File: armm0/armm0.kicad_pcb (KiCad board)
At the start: 2 copper layers, 76.2 x 52.1 mm, 10 parts, among them J1 Conn_02x10_Odd_Even, J2 Conn_02x24_Odd_Even, J3 Conn_02x24_Odd_Even, U1 STM32F070F6Px, U2 LD1117S33TR_SOT223

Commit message: armm0: Add eagle project
Signed-off-by: Ben <bdl@live.co.uk>
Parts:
- J2, J3: moved to B.Cu
- R1, R2: moved to F.Cu
- moved J2 3.81 mm to (32.4, 76.8), turned to 270 degrees
- moved C3 2.17 mm to (91.9, 52.1), turned to 0 degrees
- moved J3 1.91 mm to (32.4, 34.9), turned to 270 degrees
- turned R1 to 90 degrees
- turned R2 to 90 degrees
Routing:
- net +3V3: track 40.7 -> 9.36 mm, vias 2 -> 0
- net I2C1_SCL: track 11.3 -> 1.68 mm
- net I2C1_SDA: track 3.63 -> 1.68 mm
- net (no net): vias 1 -> 0
- added copper zone on F.Cu, net +3V3
- added copper zone on B.Cu, net GND

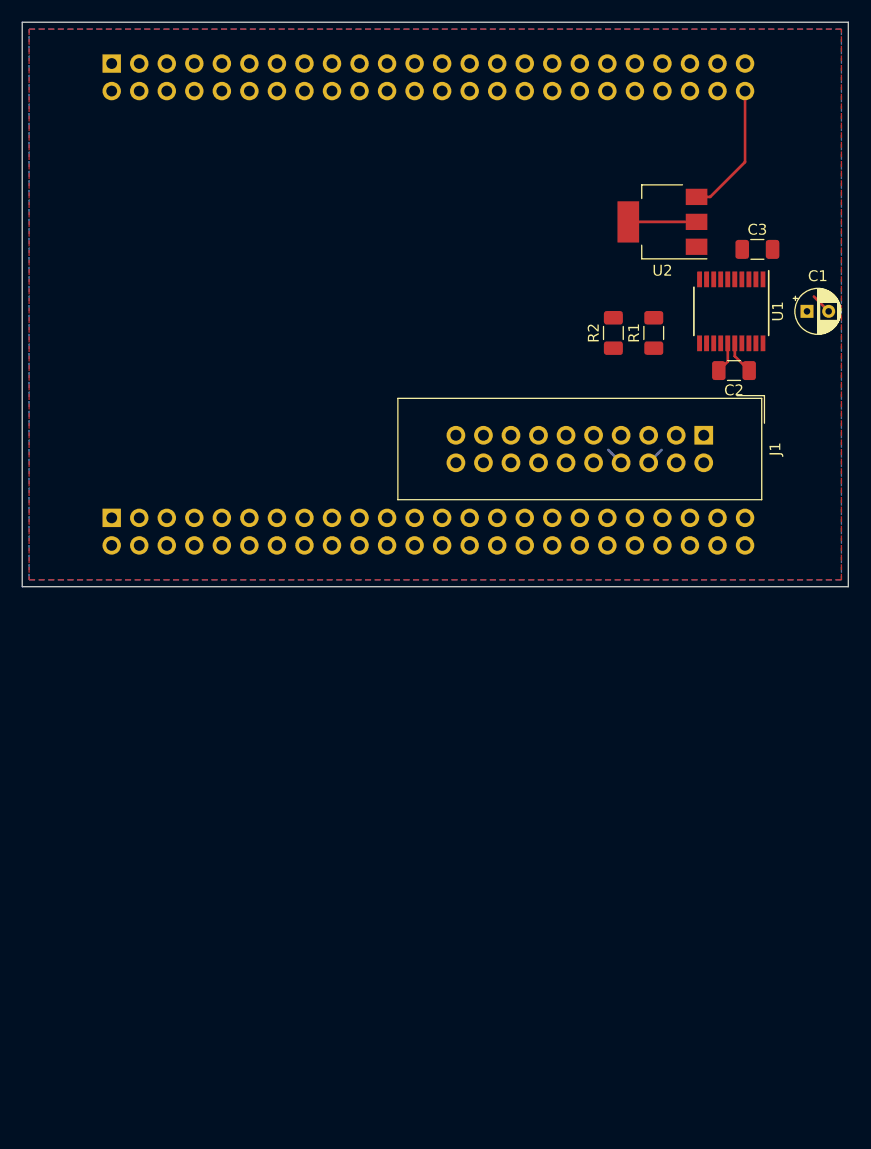
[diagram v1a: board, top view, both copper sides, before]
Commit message: sch: Add Conn_02x08 for shorter board
Signed-off-by: Ben Lancaster <bdl@live.co.uk>
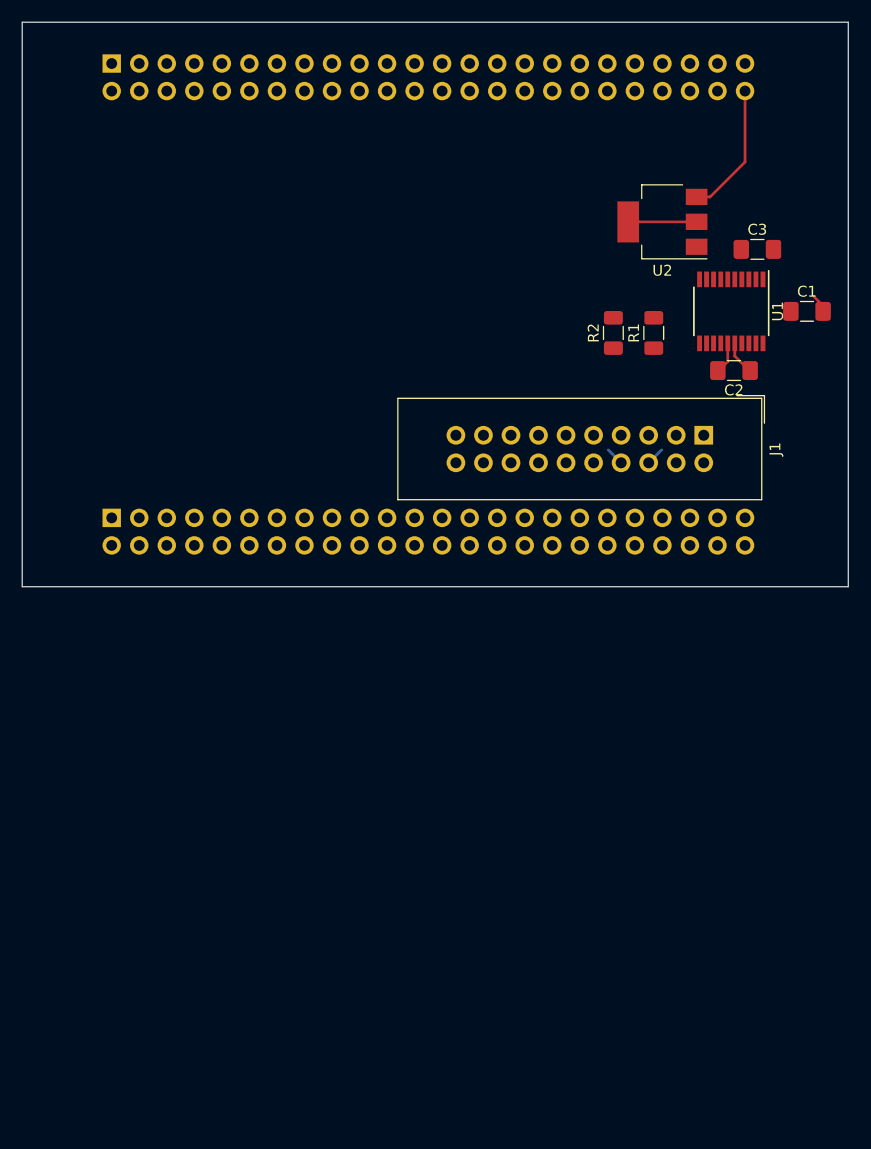
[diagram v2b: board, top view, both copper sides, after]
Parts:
- C1: footprint Capacitor_THT:CP_Radial_D4.0mm_P2.00mm -> Capacitor_SMD:C_1206_3216Metric_Pad1.42x1.75mm_HandSolder
- C2, C3: footprint Capacitor_SMD:C_1206_3216Metric -> Capacitor_SMD:C_1206_3216Metric_Pad1.42x1.75mm_HandSolder
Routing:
- removed copper zone on F.Cu, net +3V3
- removed copper zone on B.Cu, net GND

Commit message: sch: Flip Conn_02x08 pin headers for upside down insertion to master board
Signed-off-by: Ben Lancaster <bdl@live.co.uk>
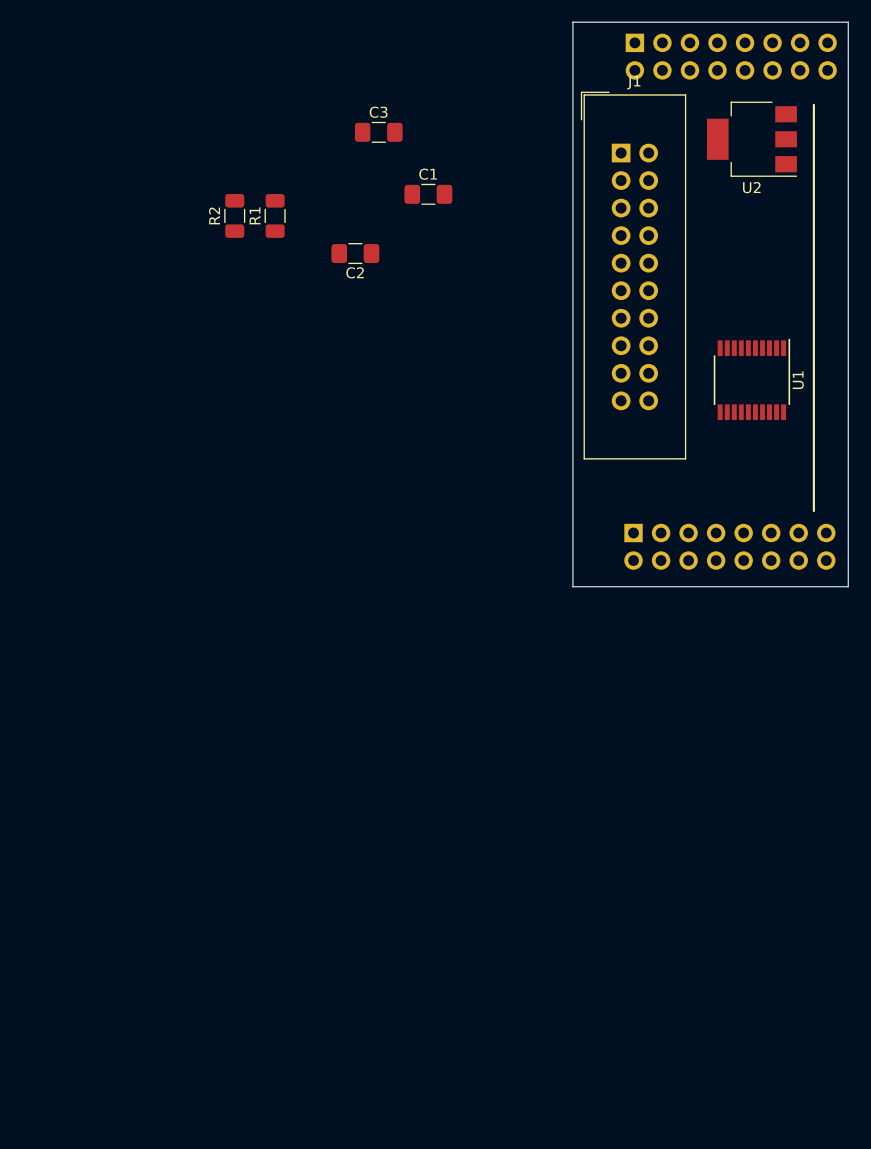
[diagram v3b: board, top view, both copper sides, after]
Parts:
- removed J2, J3: Conn_02x24_Odd_Even, Connector_PinHeader_2.54mm:PinHeader_2x24_P2.54mm_Vertical
- added J4: Conn_02x08_Odd_Even, Connector_PinHeader_2.54mm:PinHeader_2x08_P2.54mm_Vertical, B.Cu at (80.5, 78.2)
- added J5: Conn_02x08_Odd_Even, Connector_PinHeader_2.54mm:PinHeader_2x08_P2.54mm_Vertical, B.Cu at (80.6, 33.0)
- moved C2 36.6 mm to (54.9, 52.5)
- moved R1 36.6 mm to (47.5, 49.0)
- moved R2 36.6 mm to (43.7, 49.0)
- moved C1 36.6 mm to (61.6, 47.0)
- moved C3 36.6 mm to (57.0, 41.3)
- moved J1 27.1 mm to (79.4, 43.2), turned to 0 degrees
- moved U2 11.2 mm to (91.4, 41.9)
- moved U1 6.63 mm to (91.4, 64.1)
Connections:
- net Net-(J1-Pad13) renamed JTAG_TDI
- net Net-(J1-Pad3) renamed JTAG_TRST
- net Net-(J1-Pad5) renamed JTAG_TDO
- net Net-(U1-Pad6) renamed ADC_IN0
- net Net-(U1-Pad7) renamed ADC_IN1
- J1 pad 1: Net-(J1-Pad1) -> +3V3
- J1 pad 10: Net-(J1-Pad10) -> GND
- J1 pad 12: Net-(J1-Pad12) -> GND
- J1 pad 14: Net-(J1-Pad14) -> GND
- J1 pad 15: Net-(J1-Pad15) -> NRST
- J1 pad 16: Net-(J1-Pad16) -> GND
- J1 pad 18: Net-(J1-Pad18) -> GND
- J1 pad 19: Net-(J1-Pad19) -> +3V3
- J1 pad 2: SWDIO -> +3V3
- J1 pad 20: Net-(J1-Pad20) -> GND
- J1 pad 4: SWCLK -> GND
- J1 pad 6: I2C1_SDA -> GND
- J1 pad 7: Net-(J1-Pad7) -> SWDIO
- J1 pad 8: I2C1_SCL -> GND
- J1 pad 9: Net-(J1-Pad9) -> SWCLK
- R1 pad 2: I2C1_SDA -> C7
- R2 pad 2: I2C1_SCL -> C9
- U1 pad 2: I2C1_SDA -> C7
- U1 pad 3: I2C1_SCL -> C9
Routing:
- net +5V: track 13.0 -> 0.00 mm
- net +3V3: track 9.36 -> 0.00 mm
- net GND: track 4.78 -> 0.00 mm
- net I2C1_SCL: track 1.68 -> 0.00 mm
- net I2C1_SDA: track 1.68 -> 0.00 mm
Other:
- board size 76.2 x 52.1 mm -> 25.4 x 52.1 mm

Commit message: sch: Switch between board or stlink power source with 3pin selector
Signed-off-by: Ben Lancaster <bdl@live.co.uk>
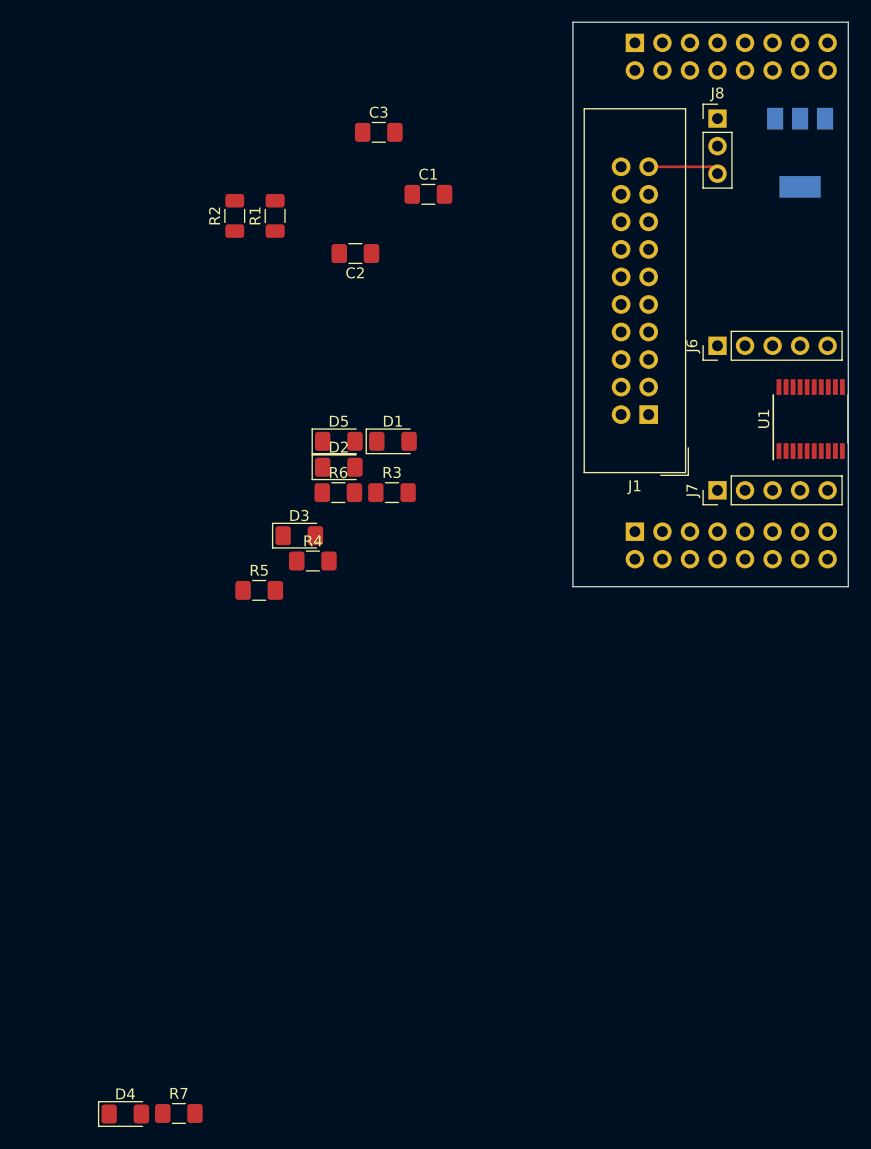
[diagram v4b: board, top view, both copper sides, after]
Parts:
- added D1: LED, LED_SMD:LED_1206_3216Metric_Pad1.42x1.75mm_HandSolder, F.Cu at (58.3, 69.8)
- added D2: LED, LED_SMD:LED_1206_3216Metric_Pad1.42x1.75mm_HandSolder, F.Cu at (53.3, 72.2)
- added D3: LED, LED_SMD:LED_1206_3216Metric_Pad1.42x1.75mm_HandSolder, F.Cu at (49.7, 78.5)
- added D4: LED, LED_SMD:LED_1206_3216Metric_Pad1.42x1.75mm_HandSolder, F.Cu at (33.6, 131.8)
- added D5: LED, LED_SMD:LED_1206_3216Metric_Pad1.42x1.75mm_HandSolder, F.Cu at (53.3, 69.8)
- added J6: Conn_01x05_Male, Connector_PinHeader_2.54mm:PinHeader_1x05_P2.54mm_Vertical, F.Cu at (88.3, 61.0)
- added J7: Conn_01x05_Male, Connector_PinHeader_2.54mm:PinHeader_1x05_P2.54mm_Vertical, F.Cu at (88.3, 74.3)
- added J8: Conn_01x03_Male, Connector_PinHeader_2.54mm:PinHeader_1x03_P2.54mm_Vertical, F.Cu at (88.3, 40.0)
- added R3: R, Resistor_SMD:R_1206_3216Metric_Pad1.42x1.75mm_HandSolder, F.Cu at (58.2, 74.5)
- added R4: R, Resistor_SMD:R_1206_3216Metric_Pad1.42x1.75mm_HandSolder, F.Cu at (50.9, 80.8)
- added R5: R, Resistor_SMD:R_1206_3216Metric_Pad1.42x1.75mm_HandSolder, F.Cu at (46.0, 83.5)
- added R6: R, Resistor_SMD:R_1206_3216Metric_Pad1.42x1.75mm_HandSolder, F.Cu at (53.3, 74.5)
- added R7: R, Resistor_SMD:R_1206_3216Metric_Pad1.42x1.75mm_HandSolder, F.Cu at (38.6, 131.8)
- U2: moved to B.Cu
- moved J1 24.3 mm to (81.9, 67.3), turned to 180 degrees
- moved U1 6.50 mm to (96.9, 67.7), turned to 90 degrees
- moved U2 4.62 mm to (95.9, 43.2), turned to 270 degrees
- moved J4 0.18 mm to (80.6, 78.1)
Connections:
- J1 pad 1: +3V3 -> STLINK_3V3
- J1 pad 19: +3V3 -> STLINK_3V3
- J1 pad 2: +3V3 -> STLINK_3V3
- J4 pad 4: F0 -> ADC_IN0
- J4 pad 6: F2 -> ADC_IN1
- U2 pad 2: +3V3 -> BOARD_3V3
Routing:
- net STLINK_3V3: track 0.00 -> 6.61 mm

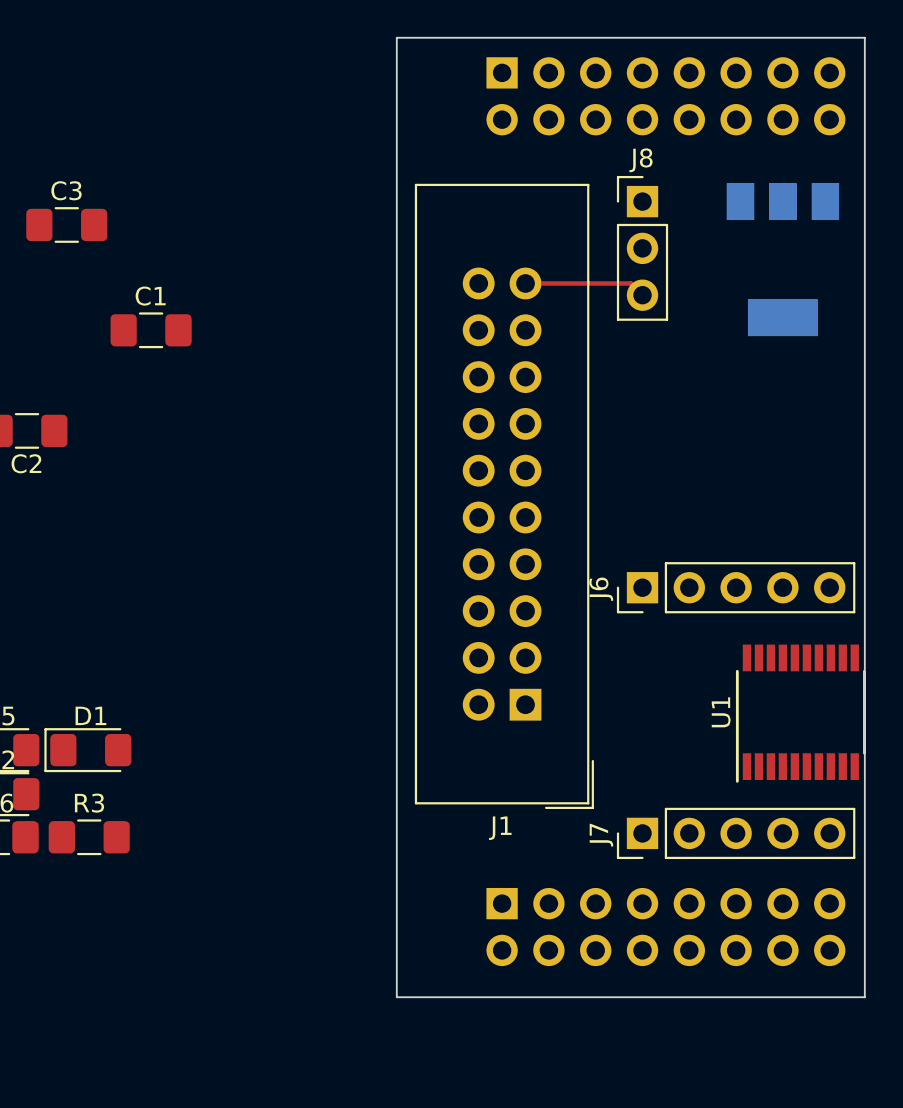
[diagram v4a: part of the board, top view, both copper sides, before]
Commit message: pcb: Some wiring done
Signed-off-by: Ben Lancaster <bdl@live.co.uk>
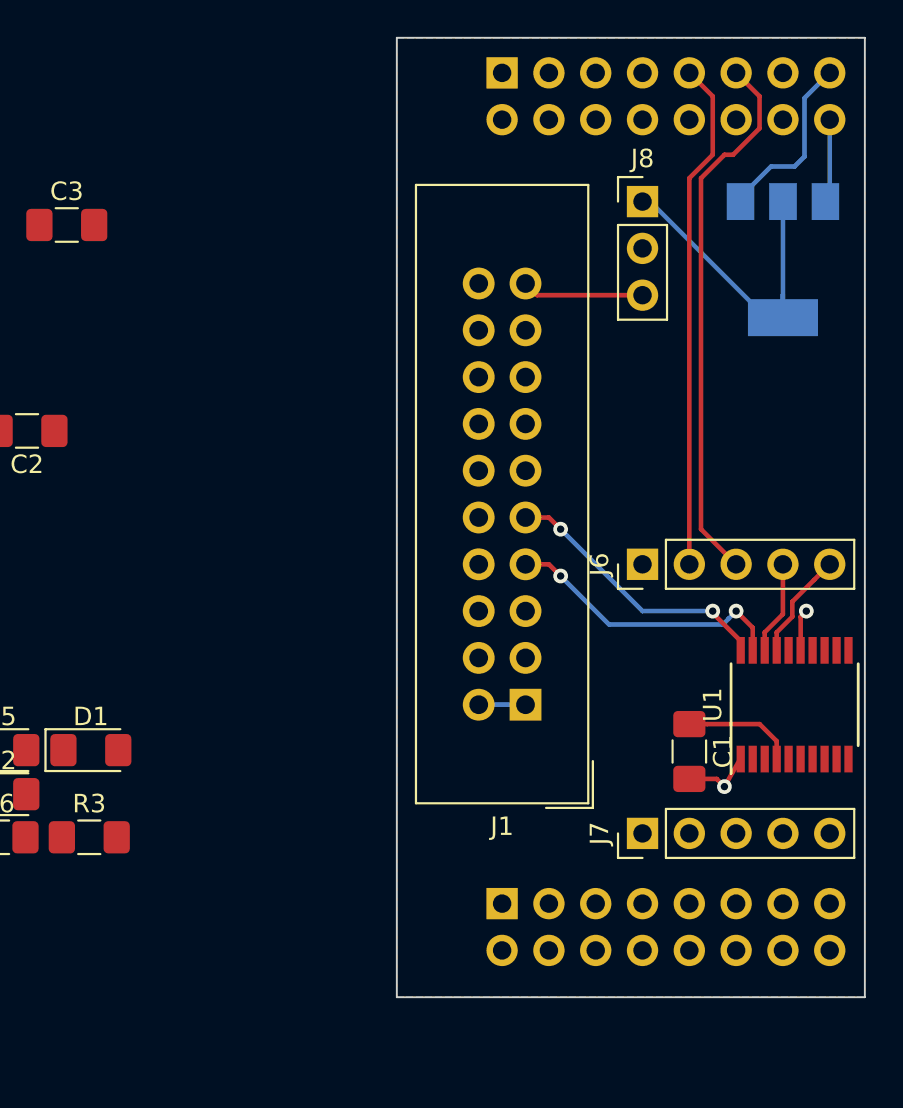
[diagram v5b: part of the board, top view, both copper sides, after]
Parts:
- moved C1 37.1 mm to (90.8, 69.8), turned to 270 degrees
- moved J6 1.27 mm to (88.3, 59.7)
- moved U1 0.53 mm to (96.5, 67.3)
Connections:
- J4 pad 10: +3V3 -> Net-(J4-Pad10)
- J4 pad 4: ADC_IN0 -> F0
- J4 pad 6: ADC_IN1 -> F2
- J5 pad 7: +3V3 -> Net-(J5-Pad7)
- J6 pad 2: C9 -> C7
- J6 pad 3: C7 -> C9
- R4 pad 1: Net-(R4-Pad1) -> +3V3
- R5 pad 1: Net-(R5-Pad1) -> +3V3
- R6 pad 1: Net-(R6-Pad1) -> +3V3
- R7 pad 1: Net-(R7-Pad1) -> +3V3
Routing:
- net C9: track 0.00 -> 29.6 mm
- net C7: track 0.00 -> 27.7 mm
- net BOARD_3V3: track 0.00 -> 18.0 mm
- net GND: track 0.00 -> 15.8 mm, vias 0 -> 2
- net SWDIO: track 0.00 -> 15.6 mm, vias 0 -> 2
- net SWCLK: track 0.00 -> 15.0 mm, vias 0 -> 2
- net NRST: track 0.00 -> 6.10 mm
- net USART1_TX: track 0.00 -> 5.86 mm
- net USART1_RX: track 0.00 -> 5.08 mm
- net +5V: track 0.00 -> 4.54 mm
- net STLINK_3V3: track 6.61 -> 9.15 mm
- added copper zone on F.Cu, net +3V3
- added copper zone on B.Cu, net GND
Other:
- net class power added: clearance 0.2, trace_width 0.35, via_dia 0.8, via_drill 0.4
- net class power5v added: clearance 0.2, trace_width 0.4, via_dia 0.8, via_drill 0.4

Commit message: pcb: Update
Signed-off-by: Ben Lancaster <bdl@live.co.uk>
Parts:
- R1, R2: moved to B.Cu
- moved R2 50.7 mm to (94.5, 48.9), turned to 180 degrees
- moved R1 47.1 mm to (94.5, 51.4), turned to 180 degrees
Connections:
- net C7 renamed I2C1_SDA
- net C9 renamed I2C1_SCL
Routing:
- net NRST: track 6.10 -> 31.2 mm
- net I2C1_SCL: track 29.6 -> 53.5 mm, vias 0 -> 2
- net I2C1_SDA: track 27.7 -> 50.2 mm, vias 0 -> 2
- net +3V3: track 0.00 -> 5.23 mm, vias 0 -> 1
